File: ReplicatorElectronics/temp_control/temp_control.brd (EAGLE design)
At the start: 44.5 x 42.2 mm, 10 parts, among them J1 SBH11-PBPC-D05-ST-BK, J2 OSTVN04A150, Q1 IRL540N, T1 MMBT2222A, T2 MMBT2222A, T3 MMBT3906LT1

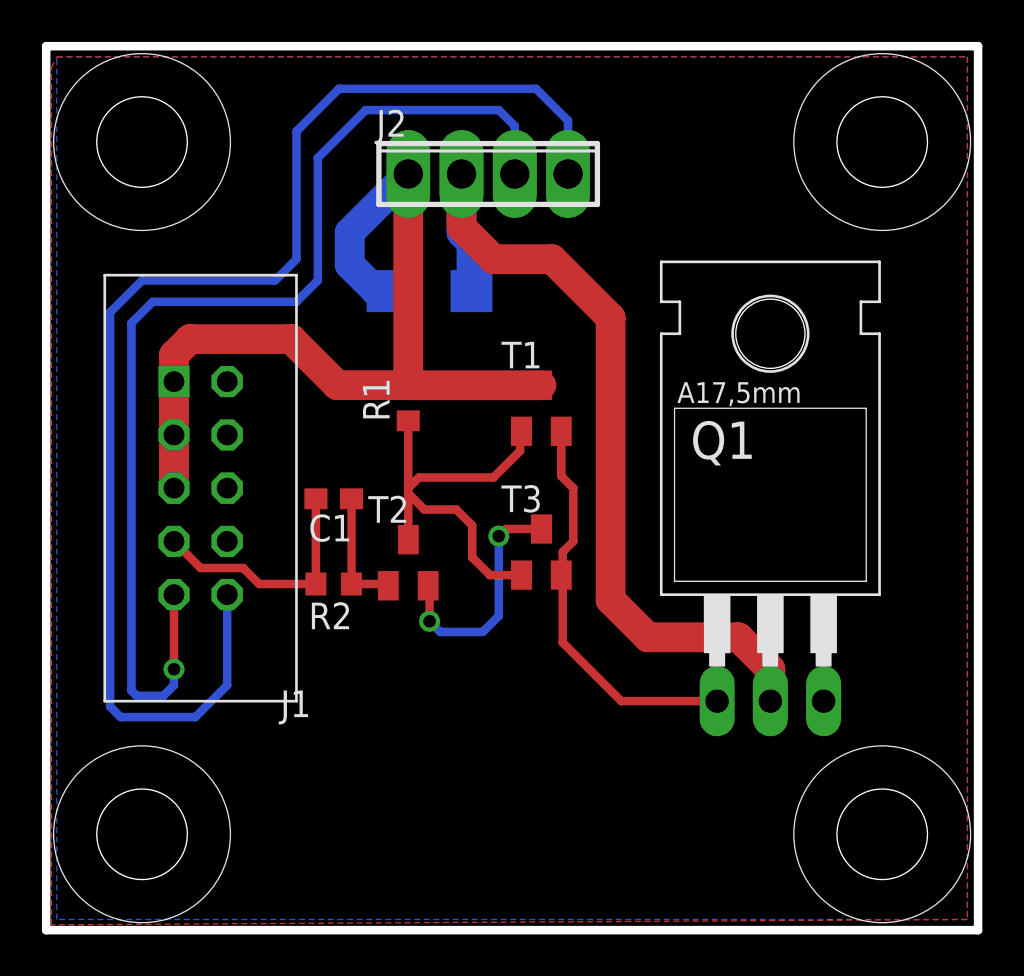
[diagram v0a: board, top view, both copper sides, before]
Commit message: 5/25/12: Brought all components topside, some minor cleanup. No change to placement of holes or large components.
~ 0.5 hr.
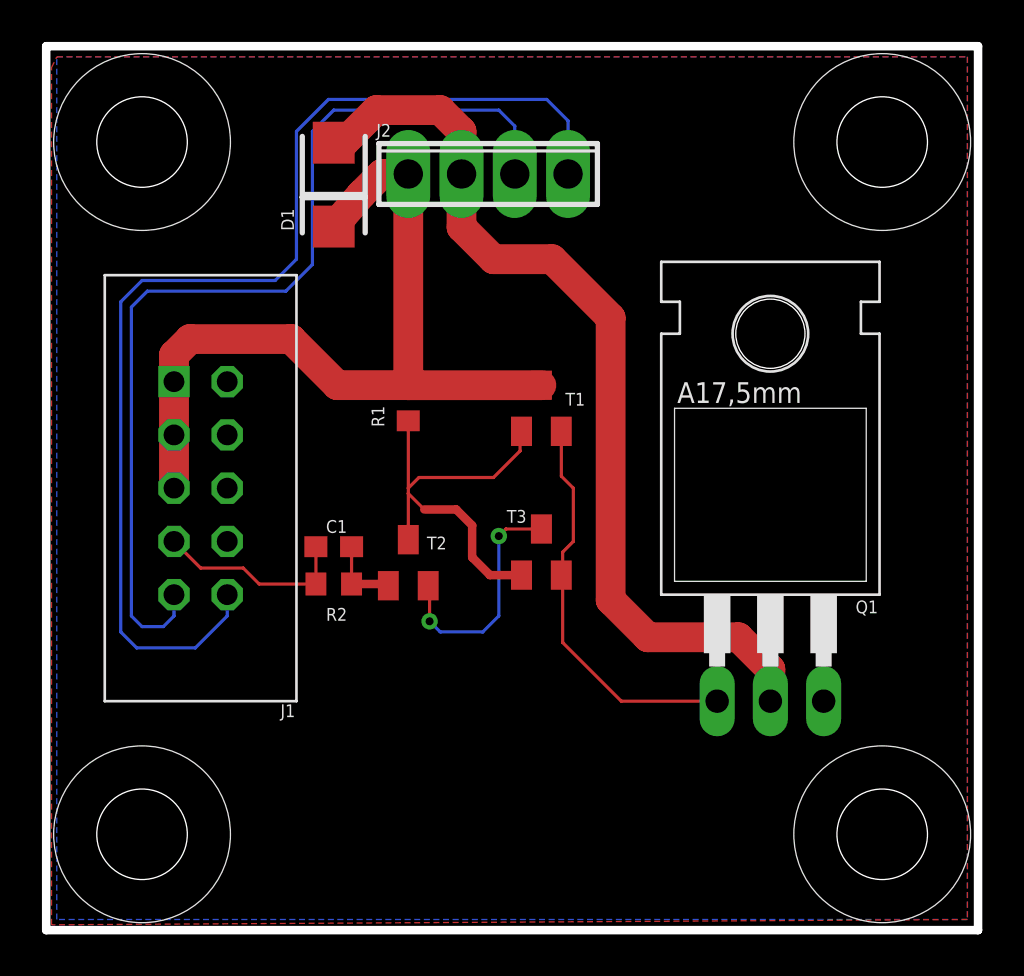
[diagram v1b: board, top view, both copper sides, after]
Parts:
- moved D1 6.83 mm to (13.7, 35.8), flipped to the top, turned to 90 degrees
- moved C1 2.29 mm to (13.7, 18.5)
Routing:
- net THERM2: track 62.5 -> 54.7 mm
- net THERM1: track 52.7 -> 46.7 mm, vias 1 -> 0
- net HEAT0: track 41.2 -> 44.6 mm
- net VCC: track 43.0 -> 39.8 mm
- net N$3: track 6.16 -> 3.87 mm
- net CTRL: track 11.7 -> 9.39 mm

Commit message: 6/3/12: Added LED.
~ 0.5 hr.
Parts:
- added LED1: RED, resistor:R0603
- added R3: 3.9k, resistor:R0603
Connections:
- new net N$1: LED1.2, R3.1
- net GND: now also LED1.1
- net N$6: now also R3.2
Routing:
- net N$6: track 19.1 -> 22.8 mm
- net N$1: track 0.00 -> 3.13 mm
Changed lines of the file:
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@@
 <attribute name="NAME" x="11.176" y="10.414" size="0.6096" layer="25" font="vector"/>
+</element>
+<element name="R3" library="resistor" package="R0603" value="3.9k" x="31.242" y="7.62" smashed="yes">
+<attribute name="NAME" x="30.861" y="5.969" size="0.6096" layer="25" font="vector"/>
+</element>
+<element name="LED1" library="resistor" package="R0603" value="RED" x="26.416" y="7.62" smashed="yes">
+<attribute name="NAME" x="25.527" y="5.969" size="0.6096" layer="25" font="vector"/>
 </element>
 </elements>
@@
 <contactref element="J1" pad="6"/>
 <contactref element="J1" pad="8"/>
+<contactref element="LED1" pad="1"/>
 </signal>
 <signal name="THERM1">
@@
 <wire x1="24.638" y1="13.97" x2="27.432" y2="11.176" width="0.1524" layer="1"/>
 <wire x1="27.432" y1="11.176" x2="32.004" y2="11.176" width="0.1524" layer="1"/>
+<contactref element="R3" pad="2"/>
+<wire x1="32.004" y1="11.176" x2="32.092" y2="11.176" width="0.1524" layer="1"/>
+<wire x1="32.092" y1="11.176" x2="32.092" y2="7.62" width="0.1524" layer="1"/>
 </signal>
 <signal name="N$8">
@@
 <wire x1="16.256" y1="16.68" x2="16.256" y2="16.764" width="0.4064" layer="1"/>
 </signal>
+<signal name="N$1">
+<contactref element="R3" pad="1"/>
+<contactref element="LED1" pad="2"/>
+<wire x1="30.392" y1="7.62" x2="27.266" y2="7.62" width="0.1524" layer="1"/>
+</signal>
 </signals>

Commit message: 5/10/12: Changed part number for Q1 to one which costs less.
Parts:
- Q1: value IRL540N -> IRL640A
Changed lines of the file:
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@@
 </autorouter>
 <elements>
-<element name="Q1" library="transistor-fet" package="TO220" value="IRL540N" x="34.544" y="17.526" smashed="yes">
+<element name="Q1" library="transistor-fet" package="TO220" value="IRL640A" x="34.544" y="17.526" smashed="yes">
 <attribute name="NAME" x="38.608" y="15.367" size="0.6096" layer="25" font="vector" ratio="10"/>
 </element>
